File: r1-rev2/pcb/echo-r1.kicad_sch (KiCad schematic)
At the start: 98 parts, among them J2 TYPE-C-31-M-12, J3 TF-115, J6 Conn_01x05, J7 ILI9342C, J8 Conn_01x04, Q4 AO3401A, Q5 AO3401A, SW1 A, SW10 SELECT, SW11 VOL+, SW12 VOL-, SW13 POWER, SW14 HOLD, SW2 B, SW3 X, SW4 Y, SW5 DPAD↑, SW6 DPAD↓, SW7 DPAD←, SW8 DPAD→, SW9 START, U10 TPAZ1143-04F, U11 TPAZ1143-04F, U12 TPAZ1143-04F, U14 USBLC6-2SC6, U7 STM32H7R3Z8Jx, U8 W958D8NBYA5I, U9 TPAZ1143-04F, Y1 SC-32S32.768kHz20PPM12.5pF, Y2 XTM32024000JT00351001

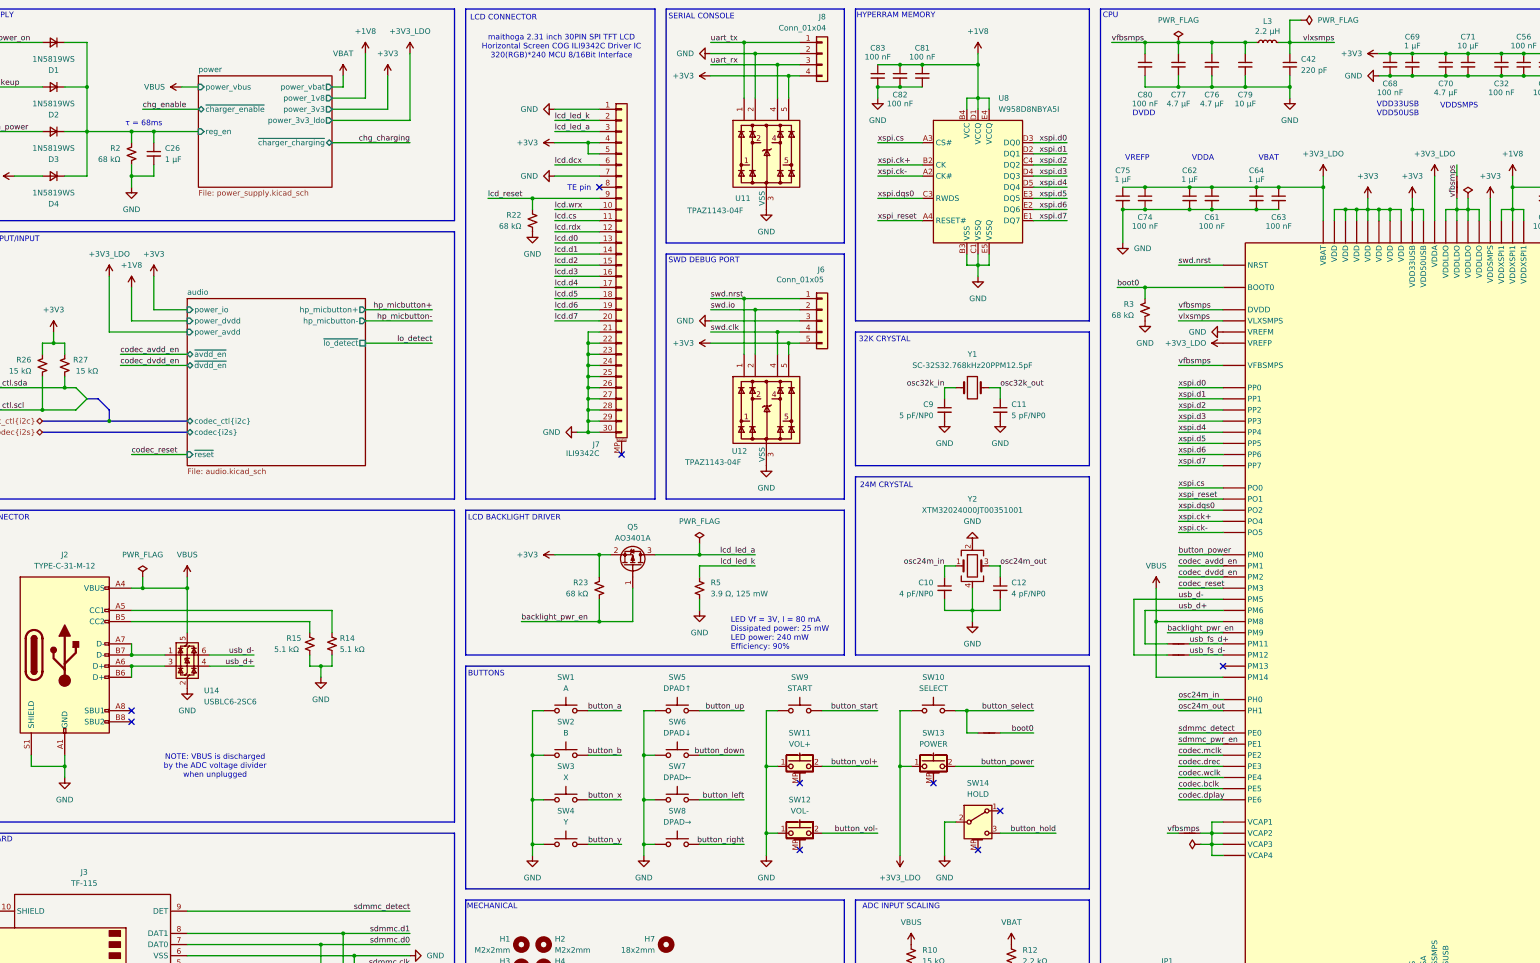
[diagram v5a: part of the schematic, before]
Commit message: R1-Rev2: update LDO power supplies for codec and RTC
The codec analog supplies (AVDD/DRVDD) are now fed through
a 3.0V LDO powered off the main 3.3V buck regulator, which
improves worst case efficiency from ~78% to around 86% and
avoids stability issues that might occur when the battery
gets within the dropout voltage range.

The new LDO (AP2125) has a very low dropout at loads well
above what the codec draws, so it should function perfectly
even at low battery levels. In theory, everything except
the memory card should still function almost all the way
down to 3.0V.

A second LDO powered from the battery is still needed just
for the RTC, but that's not too big a deal.
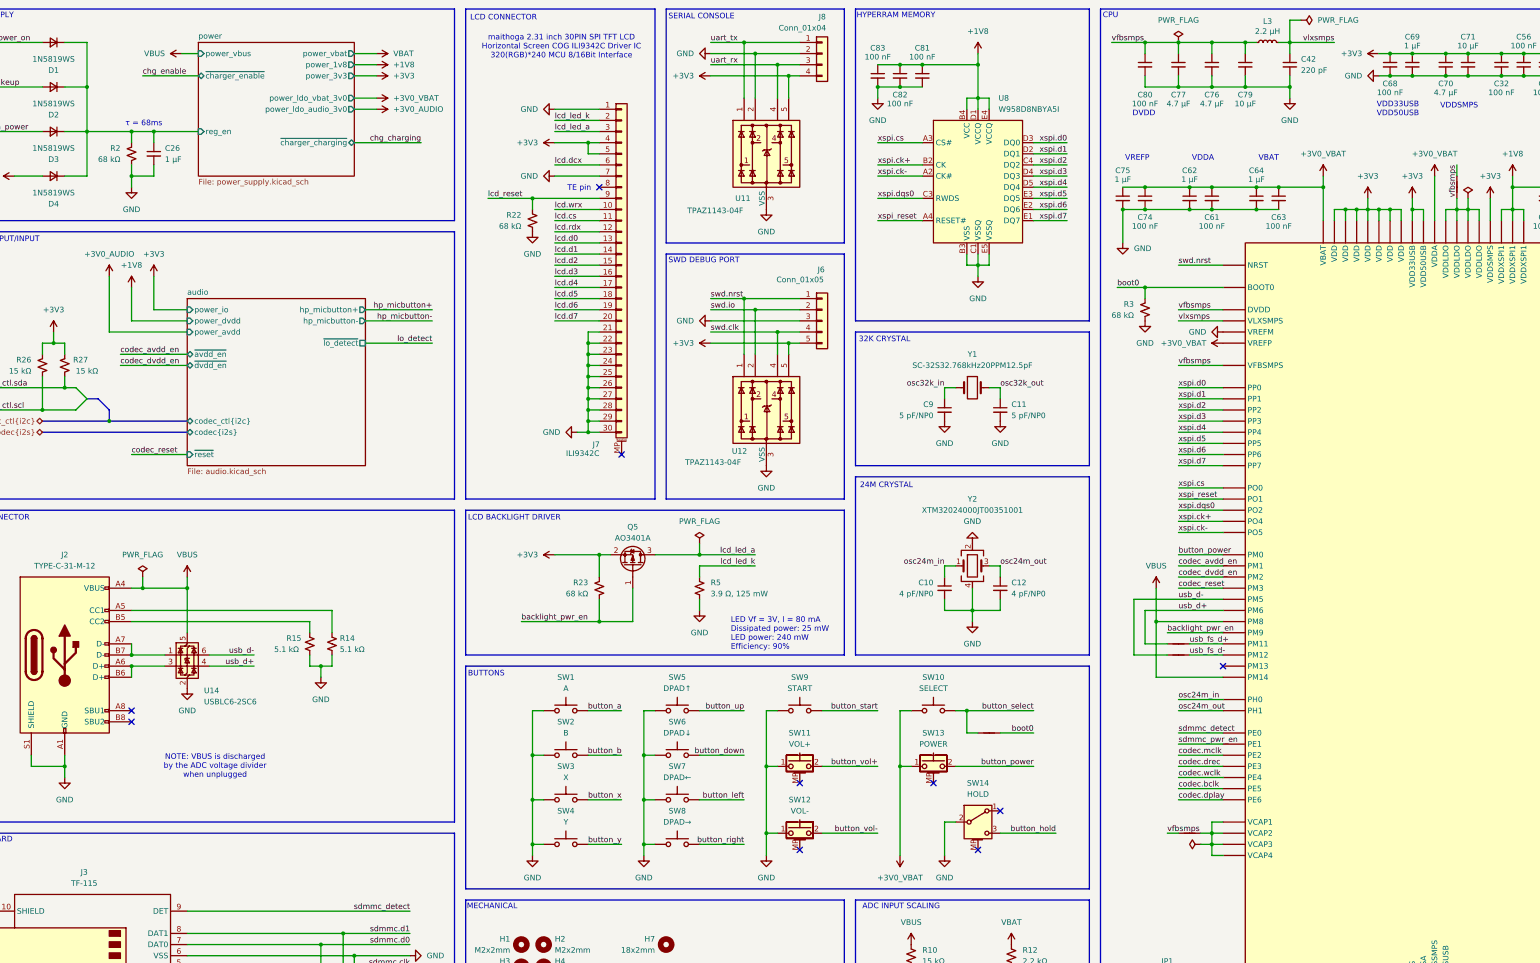
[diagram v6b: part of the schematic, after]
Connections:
- net +3V3_LDO renamed +3V0_VBAT
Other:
- sheet power ports: added power_ldo_audio_3v0, power_ldo_vbat_3v0; removed power_3v3_ldo

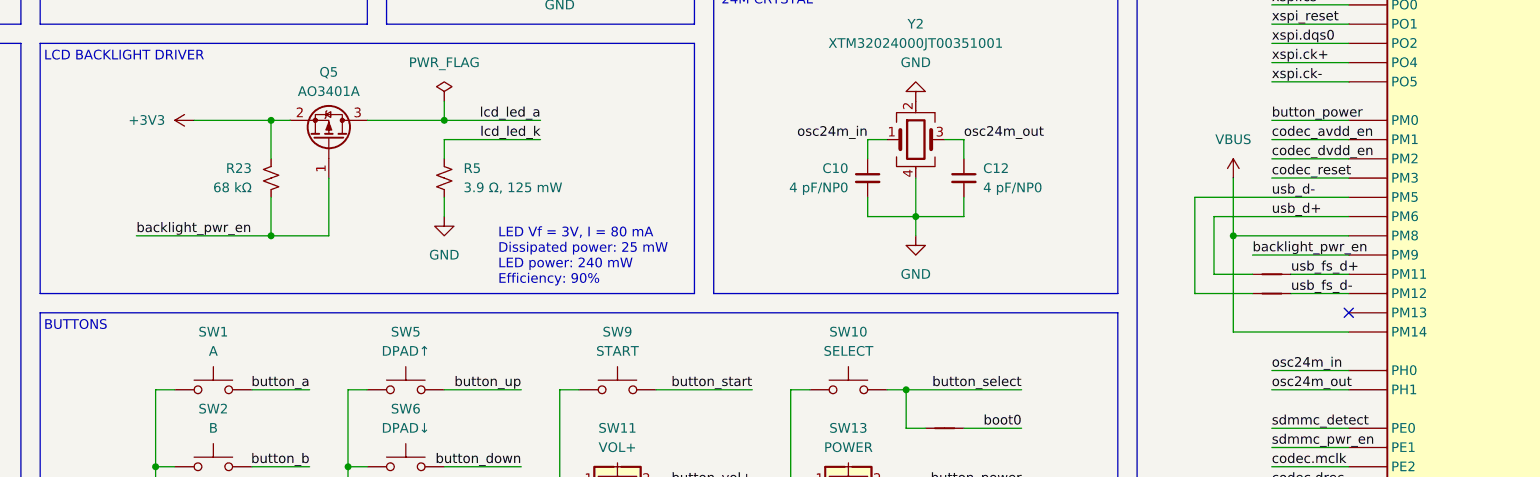
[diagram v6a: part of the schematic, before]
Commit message: R1-Rev2: fix backlight PWM connectivity
Connect PWM to the backlight driver MOSFET and remove
the unneeded backlight_pwr_en signal to free up a pin.
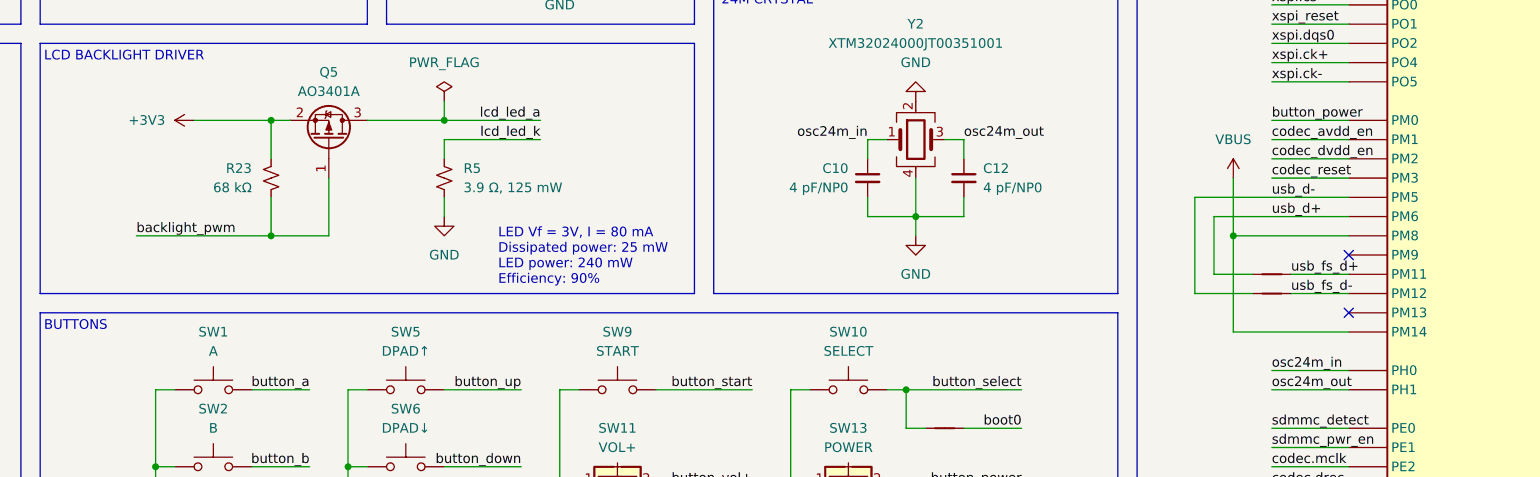
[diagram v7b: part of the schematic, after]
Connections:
- net backlight_pwm: now also Q5.1 (G), R23.2
- removed net backlight_pwr_en: Q5.1 (G), R23.2, U7.A8 (PM9)
- no-connect marks 19 -> 20

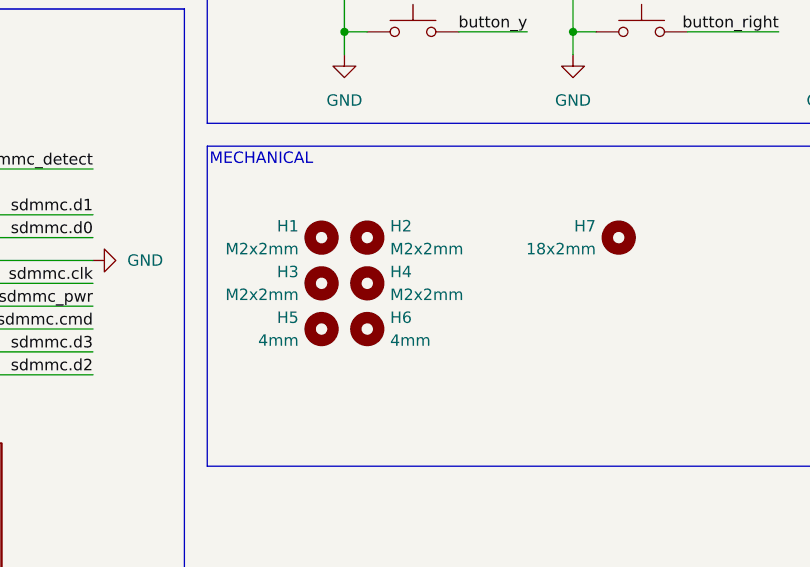
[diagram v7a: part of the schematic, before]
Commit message: R1-Rev2: change LCD ribbon cable slot placement and size
The LCD won't sit flat if the fat side of the cable is lying
underneath it because there are a bunch of capacitors there.
The cable is long enough to reach the back of the PCB though
if the entire thing is put through a slot right underneath
the screen, although it's annoyingly huge.

I've removed the screw holes there since the routing becomes
very tight in that area with them in place. Depending on how
it goes there might be room to bring one of them back or put
a screw in the middle, between the slot and the D-pad.
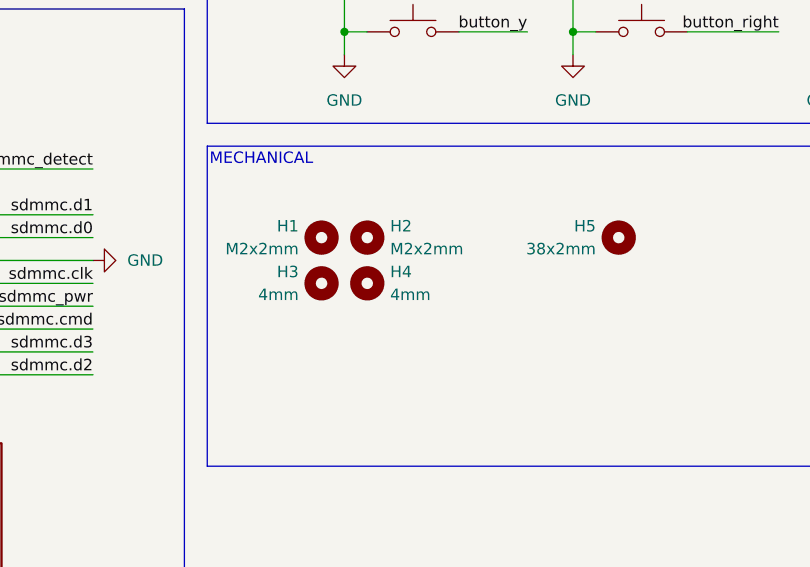
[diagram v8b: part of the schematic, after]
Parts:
- removed H3, H4: M2x2mm, MountingHole:MountingHole_2.2mm_M2, symbol Mechanical:MountingHole
- H5: renamed from H7; value 18x2mm -> 38x2mm; footprint echoplayer:Slot_18x2mm -> echoplayer:Slot_38x2mm
- renumbered H5 to H3, H6 to H4
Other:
- moved on the sheet: H3, H4
